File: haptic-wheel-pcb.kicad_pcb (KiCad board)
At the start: 2 copper layers, 6 parts, among them U1 DRV8323HRTAR

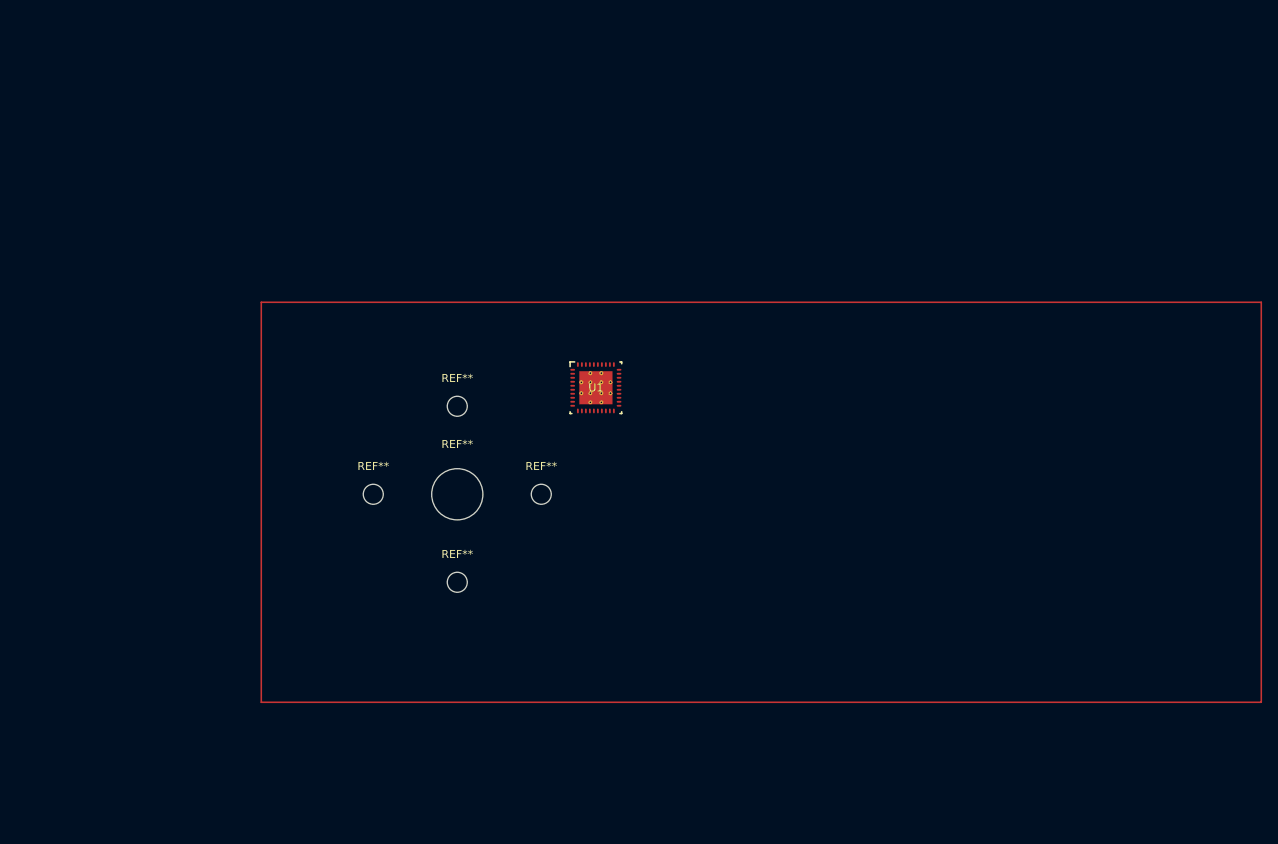
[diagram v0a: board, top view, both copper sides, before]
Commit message: routed motor driver fets and shunts
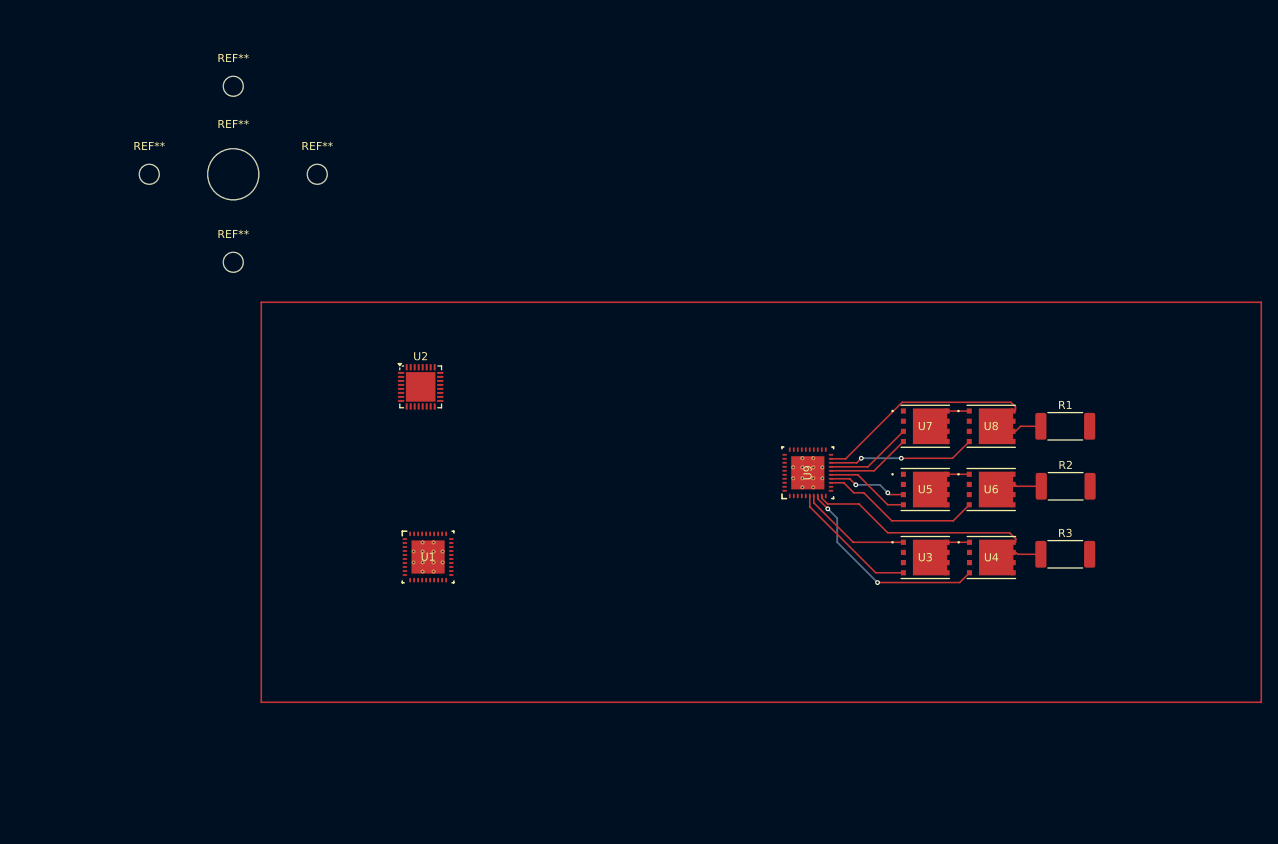
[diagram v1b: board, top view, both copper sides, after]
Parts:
- added R1: CSS2H-2512K-2L00F, Resistor_SMD:R_2512_6332Metric_Pad1.40x3.35mm_HandSolder, F.Cu at (150.5, 65.5)
- added R2: CSS2H-2512K-2L00F, Resistor_SMD:R_2512_6332Metric_Pad1.40x3.35mm_HandSolder, F.Cu at (150.6, 73.0)
- added R3: CSS2H-2512K-2L00F, Resistor_SMD:R_2512_6332Metric_Pad1.40x3.35mm_HandSolder, F.Cu at (150.5, 81.5)
- added U2: ESP32-C3, Package_DFN_QFN:QFN-32-1EP_5x5mm_P0.5mm_EP3.7x3.7mm, F.Cu at (69.9, 60.6)
- added U3: CSD18534Q5A, CSD18534Q5A:DQJ8, F.Cu at (133.0, 81.9)
- added U4: CSD18534Q5A, CSD18534Q5A:DQJ8, F.Cu at (141.3, 81.9)
- added U5: CSD18534Q5A, CSD18534Q5A:DQJ8, F.Cu at (133.0, 73.4)
- added U6: CSD18534Q5A, CSD18534Q5A:DQJ8, F.Cu at (141.2, 73.4)
- added U7: CSD18534Q5A, CSD18534Q5A:DQJ8, F.Cu at (133.0, 65.5)
- added U8: CSD18534Q5A, CSD18534Q5A:DQJ8, F.Cu at (141.2, 65.5)
- added U9: DRV8323HRTAR, DRV8323:RTA0040B, F.Cu at (118.3, 71.3)
- U1: value DRV8323HRTAR -> AS5600L-ASOM
- moved REF** 48.8 mm to (36.0, 34.0)
- moved REF** 48.8 mm to (57.0, 34.0)
- moved REF** 48.8 mm to (46.5, 23.0)
- moved REF** 48.8 mm to (46.5, 45.0)
- moved REF** 48.8 mm to (46.5, 34.0)
- moved U1 29.8 mm to (70.8, 81.8)
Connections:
- U1 pad 10: unconnected-(U1-SNA-Pad10) -> (no net)
- U1 pad 11: unconnected-(U1-SNB-Pad11) -> (no net)
- U1 pad 12: unconnected-(U1-SPB-Pad12) -> (no net)
- U1 pad 13: unconnected-(U1-GLB-Pad13) -> (no net)
- U1 pad 14: unconnected-(U1-SHB-Pad14) -> (no net)
- U1 pad 15: unconnected-(U1-GHB-Pad15) -> (no net)
- U1 pad 16: unconnected-(U1-GHC-Pad16) -> (no net)
- U1 pad 17: unconnected-(U1-SHC-Pad17) -> (no net)
- U1 pad 18: unconnected-(U1-GLC-Pad18) -> (no net)
- U1 pad 19: unconnected-(U1-SPC-Pad19) -> (no net)
- U1 pad 20: unconnected-(U1-SNC-Pad20) -> (no net)
- U1 pad 21: unconnected-(U1-SOC-Pad21) -> (no net)
- U1 pad 22: unconnected-(U1-SOB-Pad22) -> (no net)
- U1 pad 23: unconnected-(U1-SOA-Pad23) -> (no net)
- U1 pad 24: unconnected-(U1-VREF-Pad24) -> (no net)
- U1 pad 25: unconnected-(U1-FAULT_N-Pad25) -> (no net)
- U1 pad 26: unconnected-(U1-MODE_SDO-Pad26) -> (no net)
- U1 pad 27: unconnected-(U1-IDRIVE_SDI-Pad27) -> (no net)
- U1 pad 28: unconnected-(U1-VDS_SCLK-Pad28) -> (no net)
- U1 pad 29: unconnected-(U1-GAIN_SCS_N-Pad29) -> (no net)
- U1 pad 30: unconnected-(U1-ENABLE-Pad30) -> (no net)
- U1 pad 31: unconnected-(U1-CAL-Pad31) -> (no net)
- U1 pad 32: unconnected-(U1-AGND-Pad32) -> (no net)
- U1 pad 33: unconnected-(U1-DVDD-Pad33) -> (no net)
- U1 pad 34: unconnected-(U1-INHA-Pad34) -> (no net)
- U1 pad 35: unconnected-(U1-INLA-Pad35) -> (no net)
- U1 pad 36: unconnected-(U1-INHB-Pad36) -> (no net)
- U1 pad 37: unconnected-(U1-INLB-Pad37) -> (no net)
- U1 pad 38: unconnected-(U1-INHC-Pad38) -> (no net)
- U1 pad 39: unconnected-(U1-INLC-Pad39) -> (no net)
- U1 pad 40: unconnected-(U1-PGND-Pad40) -> (no net)
- U1 pad 41: unconnected-(U1-PAD-Pad41) -> (no net)
- U1 pad 9: unconnected-(U1-SPA-Pad9) -> (no net)
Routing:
- net /Motor Control/SPA: track 0.00 -> 30.3 mm
- net /Motor Control/SPC: track 0.00 -> 30.2 mm
- net Net-(U4-G): track 0.00 -> 26.0 mm, vias 0 -> 2
- net Net-(U6-G): track 0.00 -> 20.1 mm
- net Net-(U8-G): track 0.00 -> 18.4 mm, vias 0 -> 2
- net Net-(U3-G): track 0.00 -> 16.5 mm
- net Net-(U9-SHA): track 0.00 -> 14.1 mm
- net Net-(U9-SHC): track 0.00 -> 10.9 mm
- net Net-(U5-G): track 0.00 -> 10.6 mm
- net Net-(U7-G): track 0.00 -> 10.6 mm
- net Net-(U9-SHB): track 0.00 -> 9.87 mm, vias 0 -> 2
- net /Motor Control/SPB: track 0.00 -> 3.45 mm
- net /Motor Control/MOT_A: track 0.00 -> 2.48 mm
- net /Motor Control/MOT_C: track 0.00 -> 2.45 mm
- net /Motor Control/MOT_B: track 0.00 -> 2.45 mm

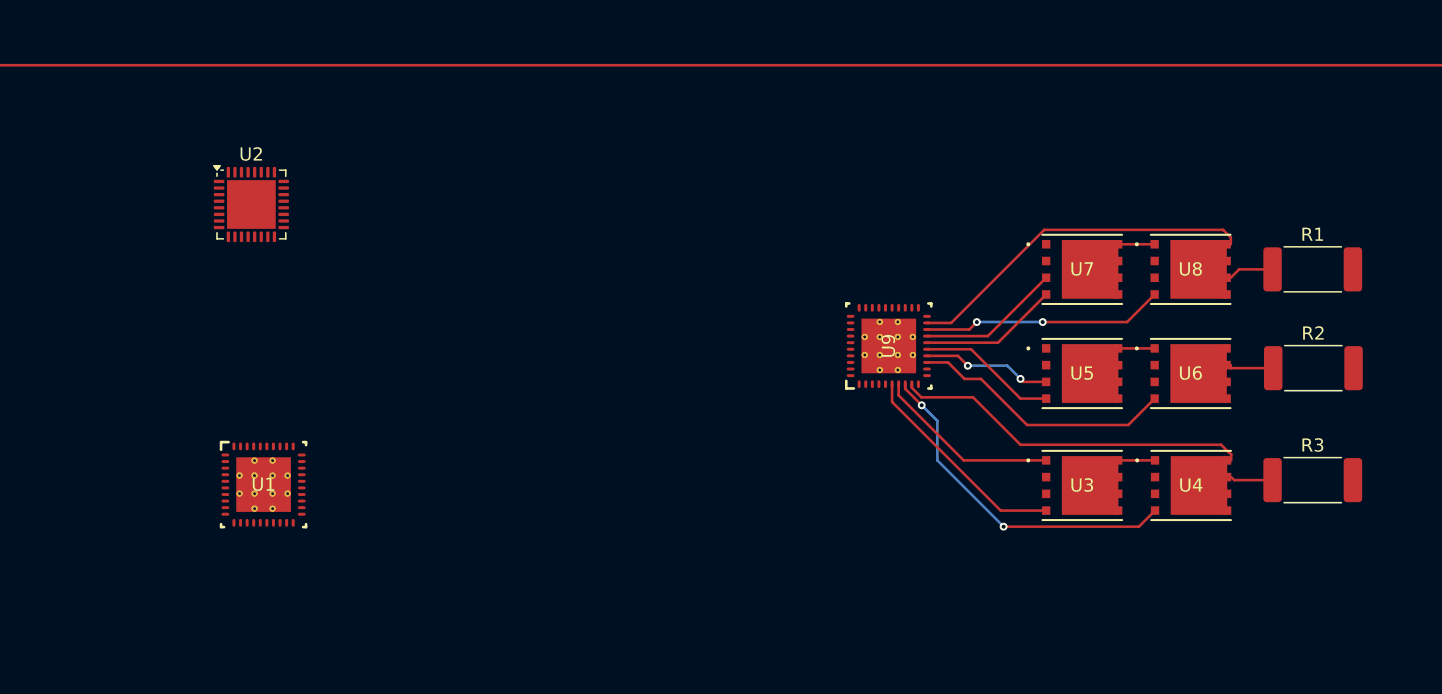
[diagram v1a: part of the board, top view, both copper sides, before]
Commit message: route all 3 fets with shunts in a vertical line
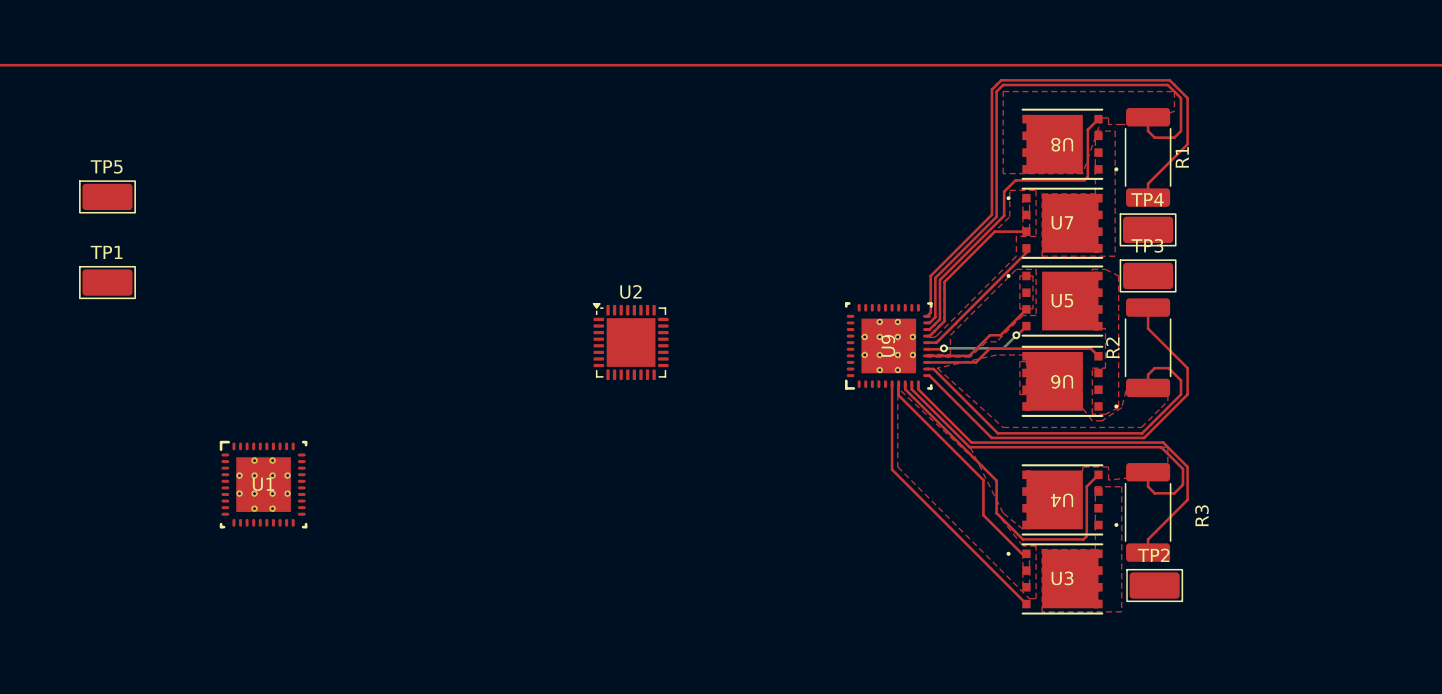
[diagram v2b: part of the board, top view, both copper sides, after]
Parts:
- added TP1: TestPoint, TestPoint:TestPoint_Keystone_5019_Miniature, F.Cu at (59.0, 66.5)
- added TP2: TestPoint, TestPoint:TestPoint_Keystone_5019_Miniature, F.Cu at (138.5, 89.5)
- added TP3: TestPoint, TestPoint:TestPoint_Keystone_5019_Miniature, F.Cu at (138.0, 66.0)
- added TP4: TestPoint, TestPoint:TestPoint_Keystone_5019_Miniature, F.Cu at (138.0, 62.5)
- added TP5: TestPoint, TestPoint:TestPoint_Keystone_5019_Miniature, F.Cu at (59.0, 60.0)
- moved U2 30.7 mm to (98.8, 71.0)
- moved R1 15.1 mm to (138.0, 57.0), turned to -90 degrees
- moved U8 13.6 mm to (131.5, 56.0), turned to 180 degrees
- moved R3 12.7 mm to (138.0, 84.0), turned to -90 degrees
- moved R2 12.6 mm to (138.0, 71.5), turned to 90 degrees
- moved U4 9.83 mm to (131.5, 83.0), turned to 180 degrees
- moved U6 9.75 mm to (131.5, 74.0), turned to 180 degrees
- moved U3 7.25 mm to (131.5, 89.0)
- moved U5 5.70 mm to (131.5, 67.9)
- moved U7 3.81 mm to (131.5, 62.0)
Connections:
- net Net-(U9-SHA) renamed /Motor Control/SHA
- net Net-(U9-SHB) renamed /Motor Control/SHB
- net Net-(U9-SHC) renamed /Motor Control/SHC
- R1 pad 2: GND -> /Motor Control/SNC
- R2 pad 2: GND -> /Motor Control/SNB
- R3 pad 2: GND -> /Motor Control/SNA
- U2 pad 11: unconnected-(U2-VDD3P3_RTC-Pad11) -> Net-(U2-VDD3P3_CPU)
- U2 pad 14: unconnected-(U2-GPIO8-Pad14) -> IO3
- U2 pad 17: unconnected-(U2-VDD3P3_CPU-Pad17) -> Net-(U2-VDD3P3_CPU)
- U2 pad 18: unconnected-(U2-VDD_SPI-Pad18) -> Net-(U2-VDD3P3_CPU)
- U2 pad 2: Net-(U2-VDD3P3-Pad2) -> Net-(U2-VDD3P3_CPU)
- U2 pad 3: Net-(U2-VDD3P3-Pad2) -> Net-(U2-VDD3P3_CPU)
- U2 pad 31: Net-(U2-VDDA-Pad31) -> Net-(U2-VDD3P3_CPU)
- U2 pad 32: Net-(U2-VDDA-Pad31) -> Net-(U2-VDD3P3_CPU)
- U2 pad 6: unconnected-(U2-GPIO2-Pad6) -> IO1
- U2 pad 8: unconnected-(U2-GPIO3-Pad8) -> IO2
- U3 pad 5: /Motor Control/MOT_A -> MOT_A
- U3 pad 6: /Motor Control/MOT_A -> MOT_A
- U3 pad 7: /Motor Control/MOT_A -> MOT_A
- U3 pad 8: /Motor Control/MOT_A -> MOT_A
- U4 pad 1: /Motor Control/MOT_A -> MOT_A
- U4 pad 2: /Motor Control/MOT_A -> MOT_A
- U4 pad 3: /Motor Control/MOT_A -> MOT_A
- U5 pad 5: /Motor Control/MOT_B -> MOT_B
- U5 pad 6: /Motor Control/MOT_B -> MOT_B
- U5 pad 7: /Motor Control/MOT_B -> MOT_B
- U5 pad 8: /Motor Control/MOT_B -> MOT_B
- U6 pad 1: /Motor Control/MOT_B -> MOT_B
- U6 pad 2: /Motor Control/MOT_B -> MOT_B
- U6 pad 3: /Motor Control/MOT_B -> MOT_B
- U7 pad 5: /Motor Control/MOT_C -> MOT_C
- U7 pad 6: /Motor Control/MOT_C -> MOT_C
- U7 pad 7: /Motor Control/MOT_C -> MOT_C
- U7 pad 8: /Motor Control/MOT_C -> MOT_C
- U8 pad 1: /Motor Control/MOT_C -> MOT_C
- U8 pad 2: /Motor Control/MOT_C -> MOT_C
- U8 pad 3: /Motor Control/MOT_C -> MOT_C
- U9 pad 10: GND -> /Motor Control/SNA
- U9 pad 11: GND -> /Motor Control/SNB
- U9 pad 20: GND -> /Motor Control/SNC
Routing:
- net /Motor Control/SNC: track 0.00 -> 44.8 mm
- net /Motor Control/SNA: track 0.00 -> 31.0 mm
- net /Motor Control/SNB: track 0.00 -> 31.0 mm
- net /Motor Control/SPB: track 3.45 -> 27.7 mm
- net /Motor Control/SPC: track 30.2 -> 42.0 mm
- net Net-(U6-G): track 20.1 -> 13.7 mm
- net Net-(U8-G): track 18.4 -> 24.5 mm, vias 2 -> 0
- net Net-(U3-G): track 16.5 -> 20.9 mm
- net /Motor Control/SHA: track 14.1 -> 17.1 mm
- net /Motor Control/MOT_A: track 2.48 -> 0.00 mm
- net /Motor Control/MOT_C: track 2.45 -> 0.00 mm
- net /Motor Control/MOT_B: track 2.45 -> 0.00 mm
- net Net-(U5-G): track 10.6 -> 8.28 mm, vias 0 -> 2
- net /Motor Control/SHC: track 10.9 -> 12.6 mm
- net /Motor Control/SPA: track 30.3 -> 28.9 mm
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- added copper zone on F.Cu, net /Motor Control/SHA
- added copper zone on F.Cu, net /Motor Control/SHB
- added copper zone on F.Cu, net /Motor Control/SHC
- added copper zone on F.Cu, net /Motor Control/SPA
- added copper zone on F.Cu, net /Motor Control/SPB
- added copper zone on F.Cu, net /Motor Control/SPC
- added copper zone on F.Cu, net MOT_A
- added copper zone on F.Cu, net MOT_B
- added copper zone on F.Cu, net MOT_C
